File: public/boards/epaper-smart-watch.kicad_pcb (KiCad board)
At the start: 4 copper layers, 41 x 36 mm, 89 parts, among them IC2 NPM1100-QDAA-R7, IC3 MAX17048G+T10, IC4 AP3032, J16 Touch3, J17 Touch2, J18 Touch1, J5 Lithium Battery 3.7V, J6 AXT624124, M1 Motor_DC, P1 USB_C_Plug_USB2.0, Q2 Si1308EDL, Q3 AO3400A, SW2 BTN, SW3 BTN, SW4 BTN, SW5 BTN, SW6 SW_Push, U1 BME280, U2 USBLC6-2SC6, U3 STM32WB5MMG, U4 XT25F32FDTIGT

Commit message: Polish portfolio interactions and e-paper showcase
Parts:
- removed BZ1: Buzzer, Jumper:SolderJumper-2_P1.3mm_Open_Pad1.0x1.5mm
- removed the C19 at (133.4, 95.5)
- added C26: 100nF, Capacitor_SMD:C_0402_1005Metric, F.Cu at (152.1, 103.2)
- added LS1: CPT-9019S-SMT-TR, SamasSys:CPT9019SSMTTR, F.Cu at (152.8, 114.8)
- added R17: 10k, Resistor_SMD:R_0402_1005Metric, F.Cu at (151.9, 98.4)
- added R18: 10k, Resistor_SMD:R_0402_1005Metric, F.Cu at (153.7, 98.7)
- added R19: 10k, Resistor_SMD:R_0402_1005Metric, F.Cu at (139.3, 96.4)
- added R20: 100k, Resistor_SMD:R_0402_1005Metric, F.Cu at (145.5, 103.0)
- L2: footprint Inductor_SMD:L_Taiyo-Yuden_NR-40xx -> Inductor_SMD:L_Taiyo-Yuden_NR-30xx
- P1: footprint USB-C-SMD_SHOU_TYPE-C-16P-CB1.6 -> ProjectLibrary:USB-C-SMD_SHOU_TYPE-C-16P-CB1.6
- Q2: footprint Package_TO_SOT_SMD:SOT-23 -> Package_TO_SOT_SMD:SOT-323_SC-70
- R5: value 8.2k -> 22k
- moved J13 23.0 mm to (142.1, 107.4)
- moved C24 16.7 mm to (154.3, 108.2), turned to 0 degrees
- moved R14 6.11 mm to (157.1, 92.6), turned to 180 degrees
- moved J17 2.73 mm to (157.0, 95.7)
- moved R11 2.21 mm to (144.9, 110.3), turned to 0 degrees
- moved C11 2.16 mm to (151.7, 107.5), turned to 0 degrees
- moved R10 1.43 mm to (146.7, 109.9)
- moved C25 1.40 mm to (157.1, 93.7)
- moved IC3 1.30 mm to (149.6, 99.1)
- moved L1 0.89 mm to (160.6, 99.3)
- moved Q2 0.85 mm to (143.6, 103.8)
- moved C23 0.85 mm to (141.5, 96.4)
- moved U3 0.80 mm to (152.2, 90.9)
- moved J7 0.78 mm to (135.1, 96.2)
- moved C3 0.72 mm to (162.2, 99.1)
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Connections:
- net /ACCL_SCL renamed /I2C_SCL
- net /ACCL_SDA renamed /I2C_SDA
- IC2 pad 4: unconnected-(IC2-NC_1-Pad4) -> GND
- U3 pad 23: /BTN_2 -> unconnected-(U3-PC11-Pad23)
- U3 pad 64: /EPD_LIGHT -> unconnected-(U3-PE1-Pad64)
- U3 pad 7: unconnected-(U3-PC3-Pad7) -> /EPD_LIGHT
- U3 pad 8: unconnected-(U3-PC2-Pad8) -> /BTN_2
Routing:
- net /SND: track 23.5 -> 37.0 mm, vias 1 -> 2
- net /NRST: track 24.7 -> 36.8 mm, vias 2 -> 3
- net +5V: track 8.59 -> 20.3 mm
- net +3V0: track 136.1 -> 143.0 mm, vias 9 -> 14
- net Net-(J6-Pin_5): track 14.3 -> 7.97 mm
- net /BTN_2: track 12.8 -> 7.12 mm
- net /FLASH_CLK: track 13.4 -> 8.35 mm
- net /FLASH_CS: track 9.00 -> 5.05 mm
- net /VSYS: track 41.3 -> 37.5 mm
- net /FLASH_IO0: track 3.38 -> 6.53 mm
- net /BTN_3: track 13.7 -> 16.8 mm
- net /BTN_1: track 25.7 -> 28.6 mm
- net /EPD_MOSI: track 33.1 -> 30.4 mm
- net /D+: track 12.6 -> 15.2 mm
- net Net-(IC2-VBAT): track 17.3 -> 14.9 mm
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- added copper zone on In1.Cu, net GND
- added copper zone on In2.Cu, net GND
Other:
- board size 41 x 36 mm -> 41.6 x 36 mm

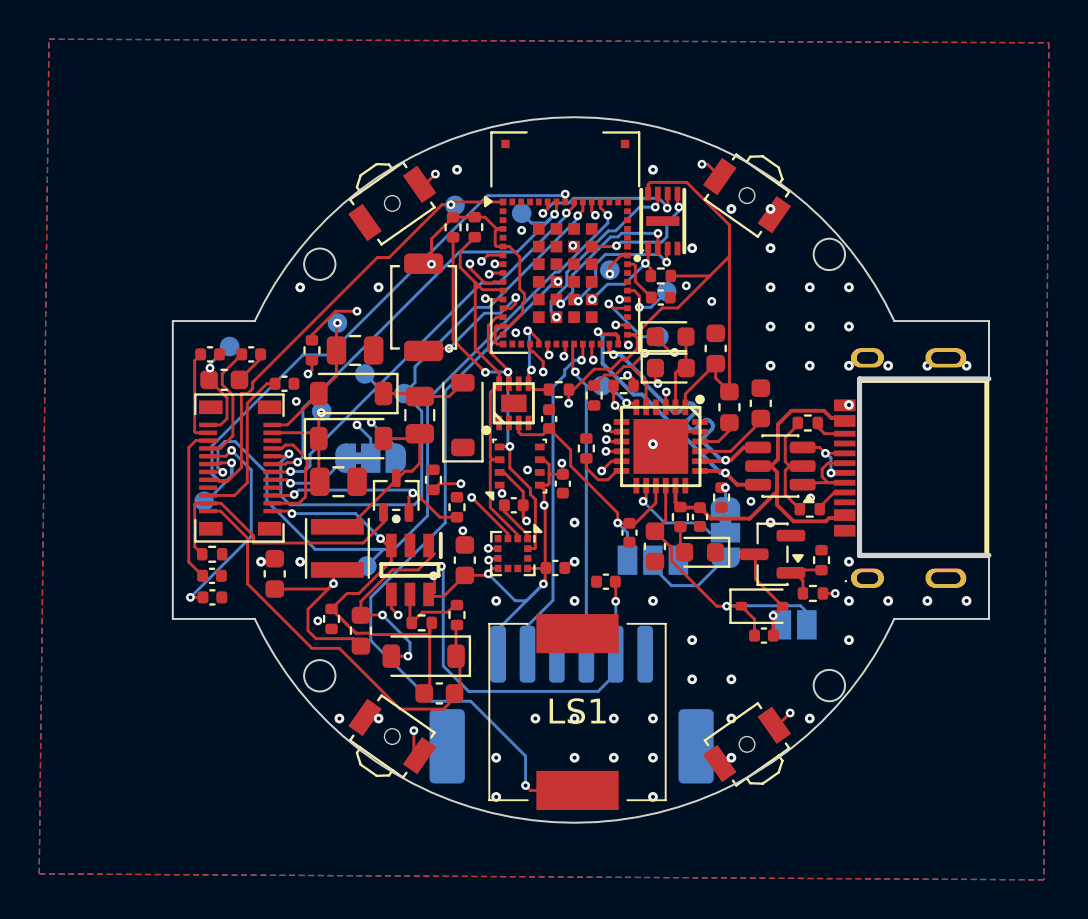
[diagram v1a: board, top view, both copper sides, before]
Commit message: Add latest e-paper PCB render
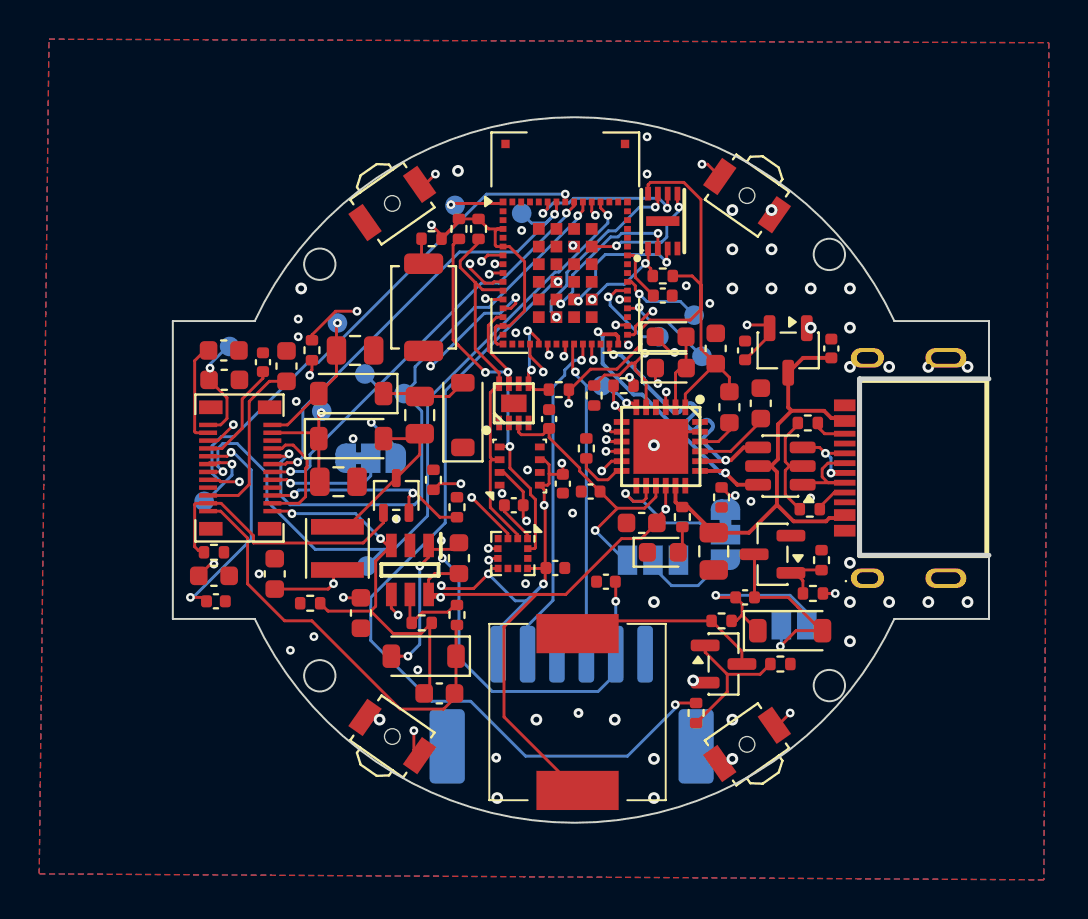
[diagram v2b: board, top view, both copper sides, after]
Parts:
- removed D4: D, Diode_SMD:D_SOD-323
- added C27: 1uF/25V, Capacitor_SMD:C_0402_1005Metric, F.Cu at (161.4, 96.4)
- added C5: 1uF/25V, Capacitor_SMD:C_0402_1005Metric, F.Cu at (165.8, 96.3)
- added D9: MBR0530, Diode_SMD:D_SOD-123, F.Cu at (163.7, 110.7)
- added Q4: AO3400A, Package_TO_SOT_SMD:SOT-23, F.Cu at (160.3, 112.4)
- added R21: 1k, Resistor_SMD:R_0402_1005Metric, F.Cu at (145.4, 90.7)
- added R22: 100, Resistor_SMD:R_0402_1005Metric, F.Cu at (158.9, 114.9)
- added R23: 100k, Resistor_SMD:R_0402_1005Metric, F.Cu at (163.2, 112.4)
- added R24: 1k, Resistor_SMD:R_0402_1005Metric, F.Cu at (160.2, 110.2)
- added U5: XC6206P332MR, Package_TO_SOT_SMD:SOT-23-3, F.Cu at (163.6, 96.4)
- C10: value 0.1uF -> 100nF/16V
- C11, C24, C25, C26, C6: value 100nF -> 100nF/16V
- C12, C9: value 0.1uF/6.3V -> 100nF/16V
- C13: value 10uF/6.3V -> 10uF/10V
- C14: value 1uF/25V -> 1uF/50V; footprint Capacitor_SMD:C_0402_1005Metric -> Capacitor_SMD:C_0603_1608Metric
- C16: value 1uF -> 1uF/50V
- C18: value 1uF/16V -> 1uF/25V
- C19, C20: value 1uF/16V -> 1uF/50V; footprint Capacitor_SMD:C_0402_1005Metric -> Capacitor_SMD:C_0603_1608Metric
- C2, C22, C3, C4: value 10uF -> 10uF/10V
- C7: value 2.2uF -> 2.2uF/25V; footprint Capacitor_SMD:C_0402_1005Metric -> Capacitor_SMD:C_0805_2012Metric
- C8: value 1uF -> 1uF/25V
- LS1: value CPT-9019S-SMT-TR -> CPT-9019B-SMT-TR
- R15: value 10 -> 100
- moved J18 6.44 mm to (159.2, 96.7)
- moved L3 6.22 mm to (146.8, 107.0)
- moved C22 5.95 mm to (141.8, 109.8), turned to -90 degrees
- moved C8 2.89 mm to (153.5, 103.6), turned to 180 degrees
- moved C9 2.17 mm to (161.4, 109.0)
- moved D3 1.90 mm to (157.2, 106.7), turned to 0 degrees
- moved C7 1.88 mm to (159.8, 106.7)
- moved J16 1.84 mm to (158.8, 94.6)
- moved C4 1.38 mm to (156.1, 105.2), turned to 180 degrees
- moved R15 1.35 mm to (139.2, 109.3), turned to 0 degrees
- moved C14 0.91 mm to (138.0, 97.2), turned to 90 degrees
- moved C20 0.73 mm to (134.8, 96.4)
- moved C18 0.72 mm to (136.8, 97.0), turned to 90 degrees
- moved R2 0.31 mm to (146.8, 90.2)
- moved C12 0.27 mm to (134.4, 109.2)
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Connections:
- C22 pad 1: +3V0 -> /VSYS
- C25 pad 1: GND -> Net-(U3-PB12)
- C25 pad 2: Net-(U3-PC13) -> GND
- IC4 pad 6: +3V0 -> /VSYS
- JP1 pad 1: Net-(J6-Pin_16) -> GND
- JP1 pad 2: GND -> Net-(J6-Pin_16)
- L3 pad 2: +3V0 -> /VSYS
- LS1 pad 1: GND -> Net-(Q4-D)
- LS1 pad 2: /SND -> /VSYS
- SW6 pad 1: +3V0 -> Net-(R21-Pad2)
- U3 pad 32: +3V0 -> /VUSB
- U3 pad 35: Net-(J17-Pin_1) -> Net-(J18-Pin_1)
- U3 pad 37: Net-(J16-Pin_1) -> Net-(J17-Pin_1)
- U3 pad 38: unconnected-(U3-PB15-Pad38) -> Net-(J16-Pin_1)
- U3 pad 40: Net-(U3-PC13) -> unconnected-(U3-PC13-Pad40)
- U3 pad 41: Net-(J18-Pin_1) -> Net-(U3-PB12)
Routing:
- net /VSYS: track 37.5 -> 67.6 mm, vias 3 -> 6
- net /VUSB: track 0.00 -> 10.4 mm, vias 0 -> 2
- net Net-(Q4-D): track 0.00 -> 9.95 mm
- net +3V0: track 143.0 -> 134.6 mm
- net Net-(Q4-G): track 0.00 -> 7.50 mm
- net /SND: track 37.0 -> 42.7 mm
- net +5V: track 20.3 -> 24.9 mm
- net Net-(D9-A): track 5.54 -> 9.98 mm
- net GND: track 19.2 -> 15.6 mm, vias 70 -> 60
- net Net-(J18-Pin_1): track 1.51 -> 4.94 mm
- net /EPD_SPICL: track 33.1 -> 29.8 mm
- net Net-(U3-PB12): track 0.00 -> 2.79 mm
- net Net-(U3-PC13): track 2.40 -> 0.00 mm
- net Net-(J6-Pin_5): track 7.97 -> 10.2 mm, vias 0 -> 2
- net Net-(IC2-NTC): track 5.72 -> 7.90 mm
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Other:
- board text added: "JLCJLCJLCJLC"

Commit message: Polish project galleries and optimise media
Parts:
- added C28: 100nF/16V, Capacitor_SMD:C_0402_1005Metric, F.Cu at (158.8, 90.1)
- D1, D2, D3: value LED -> LED White
- J6: value AXT624124 -> AXT524124; footprint ProjectLibrary:AXT624124 -> ProjectLibrary:PANASONIC_AXT524124
- R10: footprint Resistor_SMD:R_0402_1005Metric -> Resistor_SMD:R_0603_1608Metric
- SW2, SW3, SW4, SW5: footprint Button_Switch_SMD:SW_SPST_B3U-3000P-B -> Button_Switch_SMD:SW_SPST_B3U-3000P
- moved C19 11.2 mm to (136.7, 97.0), turned to 90 degrees
- moved J11 4.50 mm to (133.9, 99.6)
- moved C16 3.46 mm to (145.8, 110.4)
- moved R13 3.04 mm to (153.0, 100.3), turned to 0 degrees
- moved R10 2.91 mm to (146.9, 107.0)
- moved J4 2.72 mm to (155.7, 100.4)
- moved C18 2.44 mm to (138.2, 95.0), turned to 0 degrees
- moved L3 2.38 mm to (146.2, 104.7), turned to 0 degrees
- moved R9 2.28 mm to (145.3, 102.6), turned to 180 degrees
- moved R20 1.75 mm to (147.2, 102.6), turned to 180 degrees
- moved R11 1.50 mm to (143.4, 110.3), turned to 180 degrees
- moved C12 1.30 mm to (134.4, 107.9)
- moved R5 1.22 mm to (153.5, 102.6), turned to 0 degrees
- moved C21 0.47 mm to (134.4, 97.7)
- moved J6 0.46 mm to (135.6, 102.4), turned to -90 degrees
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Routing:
- net /SND: track 42.7 -> 32.5 mm
- net Net-(P1-D--PadA7): track 4.51 -> 9.70 mm
- net /EPD_LIGHT_PWR_NEG: track 21.6 -> 16.7 mm
- net Net-(J6-Pin_5): track 10.2 -> 6.01 mm
- net Net-(J6-Pin_7): track 5.50 -> 9.49 mm, vias 0 -> 2
- net Net-(J6-Pin_19): track 8.89 -> 12.5 mm, vias 0 -> 2
- net +3V0: track 134.6 -> 137.9 mm, vias 14 -> 16
- net /EPD_BUSY: track 23.4 -> 25.3 mm
- net Net-(P1-CC1): track 1.55 -> 3.34 mm
- net /EPD_SPICL: track 29.8 -> 28.2 mm
- net Net-(IC2-ICHG): track 2.48 -> 1.11 mm
- net Net-(IC4-OV): track 4.17 -> 5.50 mm
- net /EPD_RESR: track 11.2 -> 9.89 mm
- net /EPD_LIGHT: track 25.7 -> 24.4 mm
- net /VSYS: track 67.6 -> 68.9 mm
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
